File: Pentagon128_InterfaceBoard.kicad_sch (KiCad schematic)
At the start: 34 parts, among them J1 DIN41612_02x32_AB, J10 Tape Out, J11 Tape In, J12 Mini-DIN-6, J13 Conn_02x05_Odd_Even ATmega Pr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, J2 Conn_02x03_Odd_Even ATmega Pr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, J3 Conn_02x08_Odd_Even Ext Keyb, J4 Conn_02x05_Odd_Even Kempston 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, J5 DE9_Plug Kempston Out SMD, J6 DE15_Plug_HighDensity VGA CRT, J7 Conn_01x04 FDD Power, J8 Conn_01x04 Audio In, J9 AudioJack3, Q1 Q_NPN_BCE, Q2 Q_NPN_BCE, Q3 Q_NPN_BCE, Q4 Q_NPN_BCE, U1 MT8816 PLCC44, U2 ATmega168PA-A

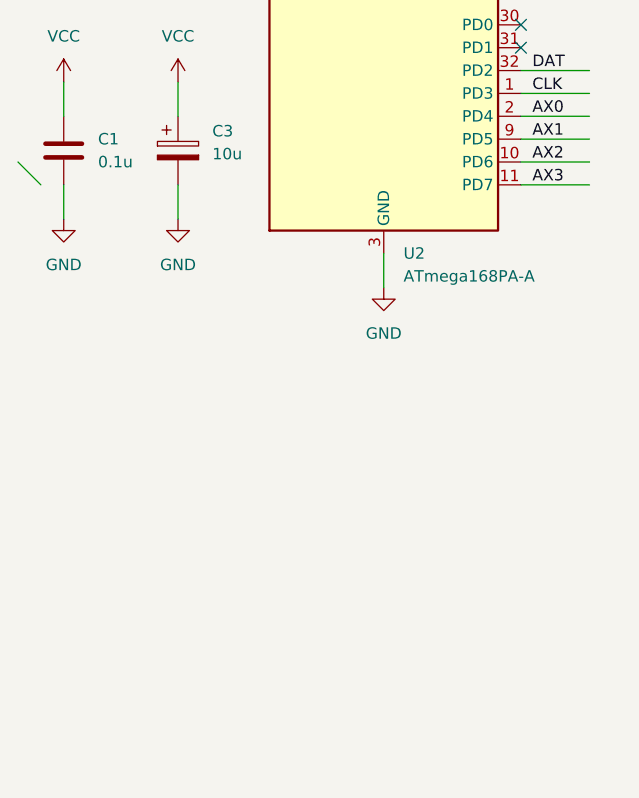
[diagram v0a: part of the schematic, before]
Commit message: Add 5.5x2.1mm 5V DC external power connector.
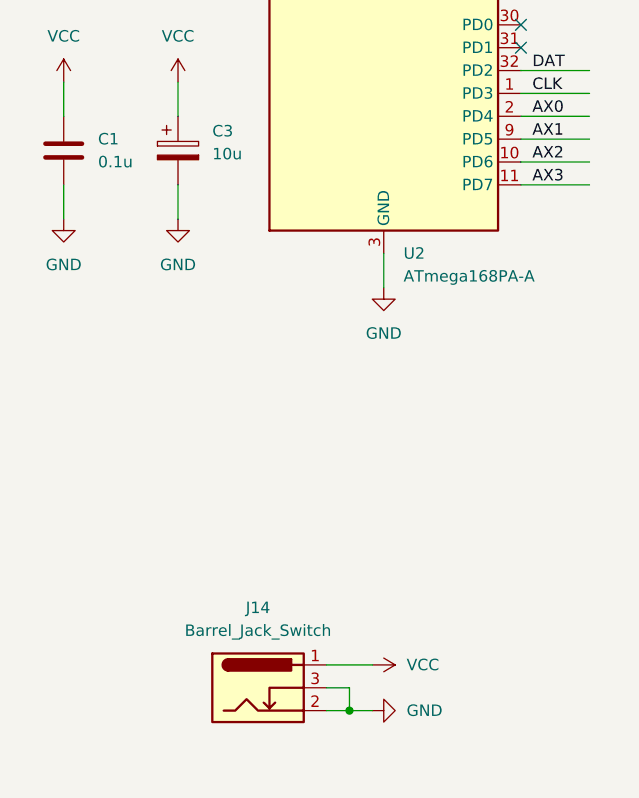
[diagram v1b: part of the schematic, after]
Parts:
- added J14: Barrel_Jack_Switch, Connector_BarrelJack:BarrelJack_Horizontal, symbol Connector:Barrel_Jack_Switch
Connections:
- net GND: now also J14.2, J14.3
- net VCC: now also J14.1
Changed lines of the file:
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@@
   (junction (at 104.14 91.44) (diameter 0) (color 0 0 0 0)
+  )
+  (junction (at 48.26 179.07) (diameter 0) (color 0 0 0 0)
   )
   (junction (at 261.62 76.2) (diameter 0) (color 0 0 0 0)
@@
   (no_connect (at 124.46 160.02))
   (no_connect (at 176.53 66.04))
-  (bus_entry (at 11.43 118.11) (size 2.54 2.54)
-    (stroke (width 0) (type default))
-  )
   (wire (pts (xy 219.71 33.02) (xy 222.25 33.02))
     (stroke (width 0) (type default))
@@
     (stroke (width 0) (type default))
   )
+  (wire (pts (xy 45.72 173.99) (xy 50.8 173.99))
+    (stroke (width 0) (type default))
+  )
   (wire (pts (xy 104.14 157.48) (xy 104.14 160.02))
     (stroke (width 0) (type default))
@@
     (stroke (width 0) (type default))
   )
+  (wire (pts (xy 45.72 176.53) (xy 48.26 176.53))
+    (stroke (width 0) (type default))
+  )
   (wire (pts (xy 124.46 104.14) (xy 134.62 104.14))
     (stroke (width 0) (type default))
@@
     (stroke (width 0) (type default))
   )
+  (wire (pts (xy 45.72 179.07) (xy 48.26 179.07))
+    (stroke (width 0) (type default))
+  )
   (wire (pts (xy 161.29 156.21) (xy 163.83 156.21))
     (stroke (width 0) (type default))
@@
     (stroke (width 0) (type default))
   )
+  (wire (pts (xy 48.26 176.53) (xy 48.26 179.07))
+    (stroke (width 0) (type default))
+  )
   (wire (pts (xy 59.69 31.75) (xy 69.85 31.75))
     (stroke (width 0) (type default))
@@
   )
   (wire (pts (xy 220.98 173.99) (xy 223.52 173.99))
+    (stroke (width 0) (type default))
+  )
+  (wire (pts (xy 48.26 179.07) (xy 50.8 179.07))
     (stroke (width 0) (type default))
   )
@@
   (label "Y6" (at 127 106.68 0) (fields_autoplaced)
     (effects (font (size 1.27 1.27)) (justify left bottom))
+  )
+  (symbol (lib_id "power:GND") (at 50.8 179.07 90) (unit 1)
+    (in_bom yes) (on_board yes) (dnp no) (fields_autoplaced)
+    (property "Reference" "#PWR021" (at 57.15 179.07 0)
+      (effects (font (size 1.27 1.27)) hide)
+    )
+    (property "Value" "GND" (at 54.61 179.07 90)
+      (effects (font (size 1.27 1.27)) (justify right))
+    )
+    (property "Footprint" "" (at 50.8 179.07 0)
+      (effects (font (size 1.27 1.27)) hide)
+    )
+    (property "Datasheet" "" (at 50.8 179.07 0)
+      (effects (font (size 1.27 1.27)) hide)
+    )
+    (pin "1")
+    (instances
+      (project "Pentagon128_InterfaceBoard"
+        (path "/fc909a4a-aded-455c-aecc-4f0751ac93b5"
+          (reference "#PWR021") (unit 1)
+        )
+      )
+    )
   )
   (symbol (lib_id "Device:Q_NPN_BCE") (at 218.44 58.42 0) (unit 1)
@@
         (path "/fc909a4a-aded-455c-aecc-4f0751ac93b5"
           (reference "#PWR05") (unit 1)
+        )
+      )
+    )
+  )
+  (symbol (lib_id "power:VCC") (at 50.8 173.99 270) (unit 1)
+    (in_bom yes) (on_board yes) (dnp no) (fields_autoplaced)
+    (property "Reference" "#PWR020" (at 46.99 173.99 0)
+      (effects (font (size 1.27 1.27)) hide)
+    )
+    (property "Value" "VCC" (at 54.61 173.99 90)
+      (effects (font (size 1.27 1.27)) (justify left))
+    )
+    (property "Footprint" "" (at 50.8 173.99 0)
+      (effects (font (size 1.27 1.27)) hide)
+    )
+    (property "Datasheet" "" (at 50.8 173.99 0)
+      (effects (font (size 1.27 1.27)) hide)
+    )
+    (pin "1")
+    (instances
+      (project "Pentagon128_InterfaceBoard"
+        (path "/fc909a4a-aded-455c-aecc-4f0751ac93b5"
+          (reference "#PWR020") (unit 1)
         )
       )
@@
         )
       )
+    )
+  )
+  (symbol (lib_id "Connector:Barrel_Jack_Switch") (at 38.1 176.53 0) (unit 1)
+    (in_bom yes) (on_board yes) (dnp no) (fields_autoplaced)
+    (property "Reference" "J14" (at 38.1 167.64 0)
+      (effects (font (size 1.27 1.27)))
+    )
+    (property "Value" "Barrel_Jack_Switch" (at 38.1 170.18 0)
+      (effects (font (size 1.27 1.27)))
+    )
+    (property "Footprint" "Connector_BarrelJack:BarrelJack_Horizontal" (at 39.37 177.546 0)
+      (effects (font (size 1.27 1.27)) hide)
+    )
+    (property "Datasheet" "~" (at 39.37 177.546 0)
+      (effects (font (size 1.27 1.27)) hide)
+    )
+    (pin "1")
+    (pin "2")
+    (pin "3")
+    (instances
+      (project "Pentagon128_InterfaceBoard"
+        (path "/fc909a4a-aded-455c-aecc-4f0751ac93b5"
+          (reference "J14") (unit 1)
+        )
+      )
